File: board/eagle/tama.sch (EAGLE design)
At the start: 35 parts, among them J1 AVR_SPI_PRG_6NS

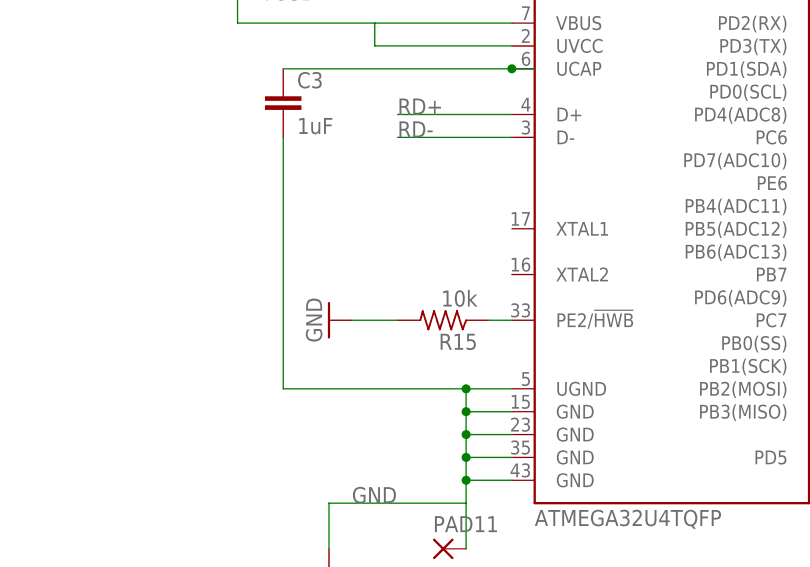
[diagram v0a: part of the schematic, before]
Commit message: Added an SMT crystal (not connected yet). Unsure if this is the right package...
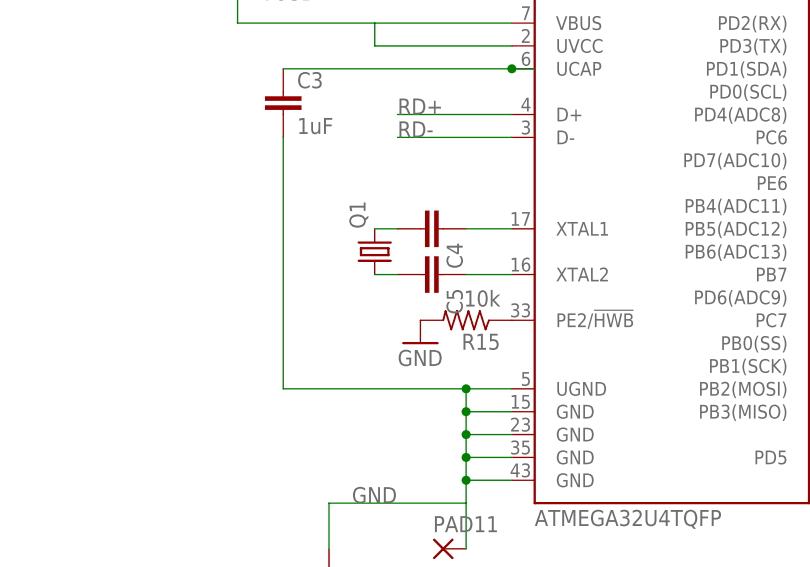
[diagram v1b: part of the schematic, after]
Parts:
- added C4, C5: (no value), SparkFun:CAP0805
- added Q1: (no value), crystal:CRYSTALCTS406
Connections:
- new net N$25: C4.2, Q1.2
- new net N$26: C5.1, U$4.XTAL2
- new net N$27: C5.2, Q1.1
- new net N$28: C4.1, U$4.XTAL1
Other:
- moved on the sheet: R15

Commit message: Redid the crystal based on the datasheet. (See pg 30 of the preliminary ATmega32U4 datasheet, doc7766.pdf)
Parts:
- C4, C5: value (none) -> 22pF
- Q1: value (none) -> 16Mhz
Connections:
- removed net N$27: C5.2, Q1.1
- removed net N$28: C4.1, U$4.XTAL1
- net GND: now also C4.2, C5.2
- net N$25: now also C4.1, U$4.XTAL1; no longer C4.2
- net N$26: now also Q1.1
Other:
- moved on the sheet: C1, C2, C3, C4, C5, C8, D1, IRGND, IRVCC, IRVO, J1, ON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
